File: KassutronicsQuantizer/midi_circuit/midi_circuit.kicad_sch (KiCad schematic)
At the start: 9 parts, among them J1 MIDI out, J2 MIDI in, U1 6N138

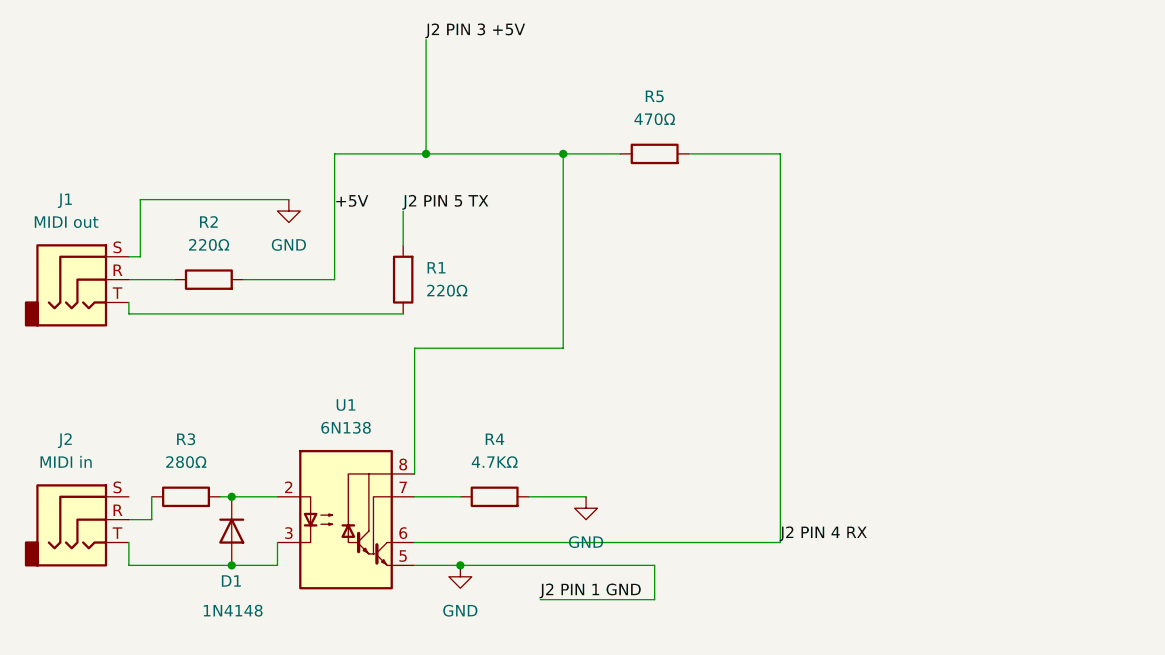
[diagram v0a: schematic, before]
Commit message: Align MIDI schematic with the KQME board
- Fix TX shorted to +5V at a junction above R1
- Add C1, 100nF between +5V and GND
- R3 is 220Ω, D1 is 1N4148W in SOD-123
- J1 is MIDI in, J2 is MIDI out, as on the board
- Note that the board carries the circuit twice

Co-Authored-By: Claude Opus 5.5 <noreply@anthropic.com>
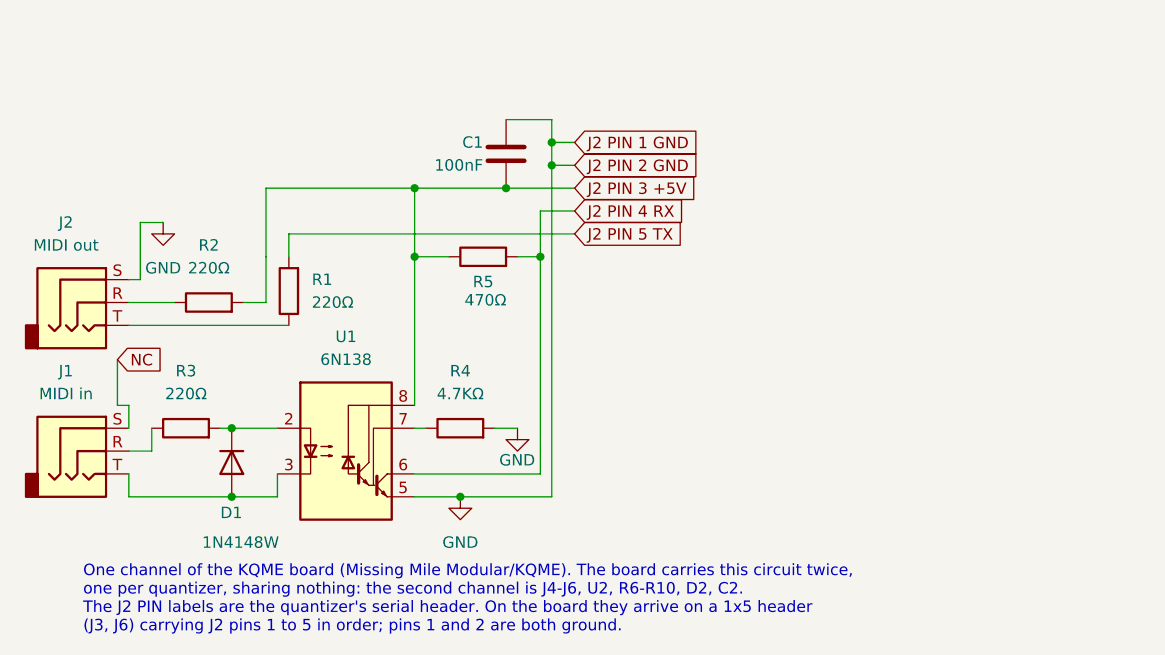
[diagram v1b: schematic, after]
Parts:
- added C1: 100nF, symbol Device:C
- D1: value 1N4148 -> 1N4148W; footprint Diode_THT:D_DO-35_SOD27_P7.62mm_Horizontal -> Diode_SMD:D_SOD-123
- R3: value 280Ω -> 220Ω
- renumbered J2 to J1, J1 to J2
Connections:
- net GND: now also C1.1
- net NC: now reaches J1.S
- net +5V renamed J2 PIN 3 +5V
- net J2 PIN 3 +5V: now also C1.2
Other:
- note added: "One channel of the KQME board (Missing Mile Modular/KQME). The board carries this circuit twice, one per quantizer, sharing nothing: the second channel is J4-J6, U2, R6-R10, D2, C2. The J2 PIN labels are the quantizer's serial header. On the board they arrive on a 1x5 header (J3, J6) carrying J2 pins 1 to 5 in order; pins 1 and 2 are both ground."
- moved on the sheet: D1, J1, J2, R1, R2, R3, R4, R5, U1
